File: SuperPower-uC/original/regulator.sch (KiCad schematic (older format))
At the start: 49 parts, among them Q10 2N7002A, Q11 2N7002A, Q13 DMP2035UVT, Q14 DMP2035UVT, Q5 DMP2035UVT, Q9 2N7002A, U10 TPS63070RNMT, U8 TPS70933DRVT, U9 TPS63070RNMT

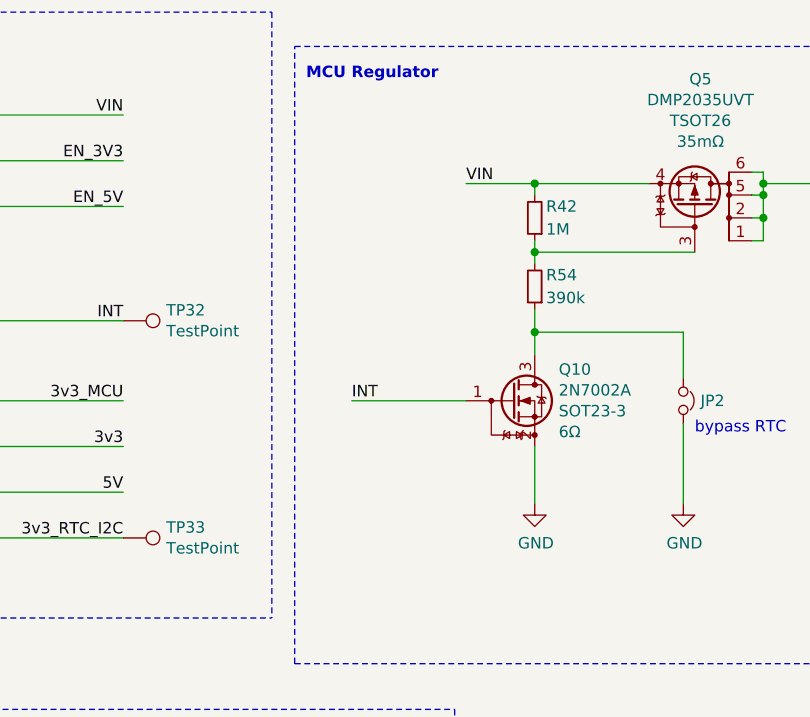
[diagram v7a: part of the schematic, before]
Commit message: Cleaned up MOSFET circuit for RTC interrupt
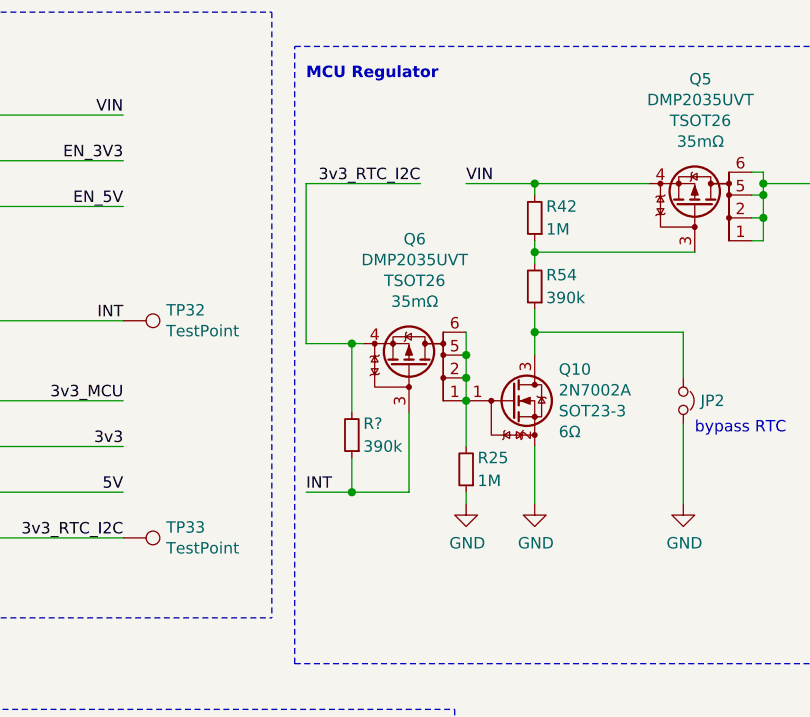
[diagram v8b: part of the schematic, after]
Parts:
- added Q6: DMP2035UVT, Package_TO_SOT_SMD:SOT-23-6, symbol dmp2035uvt:DMP2035UVT
- added R25: 1M, Resistor_SMD:R_0603_1608Metric, symbol Device:R_Small
- added R?: 390k, Resistor_SMD:R_0603_1608Metric, symbol Device:R_Small
- JP2: footprint Jumper:SolderJumper-2_P1.3mm_Open_TrianglePad1.0x1.5mm -> Connector_PinSocket_2.54mm:PinSocket_1x02_P2.54mm_Vertical
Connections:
- net 3v3_RTC_I2C: now also Q6.4 (S), R?.2
- net GND: now also R25.1
- net INT: now also Q6.3 (G), R?.1; no longer Q10.1 (G)
- new net: Q10.1 (G), Q6.1 (D), Q6.2 (D), Q6.5 (D), Q6.6 (D), R25.2
